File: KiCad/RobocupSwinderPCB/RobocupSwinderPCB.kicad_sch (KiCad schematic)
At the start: 29 parts, among them J1 Barrel_Jack, M1 Stepper_Motor_bipolar, M2 Stepper_Motor_bipolar, SW1 Limit_Switch, SW2 Limit_Switch, SW3 SW_SPST, U1 Teensy4.1, U3 LM7805_TO220

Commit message: Pcb cleanup
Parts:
- U1: footprint TeensyLibrary:Teensy41-Pins-Only_Silkscreen -> SwinderFootprintLibrary:Teensy41-Pins-Only_Silkscreen
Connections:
- net LCD_SCL_Pin_19: now also LCD1.3 (SDA); no longer LCD1.4 (SCL)
- net LCD_SDA_Pin_18: now also LCD1.4 (SCL); no longer LCD1.3 (SDA)
- net RE_CLK_Pin_23: now also RE1.3 (CLK); no longer RE1.5 (SW)
- net RE_SW_Pin_21: now also RE1.5 (SW); no longer RE1.3 (CLK)

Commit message: More pcb cleanup.
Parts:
- J1: footprint Library:CUI_PJ-037A -> SwinderFootprintLibrary:CUI_PJ-037A
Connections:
- net LCD_SCL_Pin_19: now also LCD1.4 (SCL); no longer LCD1.3 (SDA)
- net LCD_SDA_Pin_18: now also LCD1.3 (SDA); no longer LCD1.4 (SCL)
- net PWR_SW_OUT: now reaches F1.1, SW3.2 (B)
- net PWR_SW_IN: now reaches J1.1, SW3.1 (A)
- net RE_CLK_Pin_23 renamed RE_CLK_Pin_21
- net RE_CLK_Pin_21: now also U1.43 (21_A7_RX5_BCLK1); no longer U1.45 (23_A9_CRX1_MCLK1)
- net RE_SW_Pin_21 renamed RE_SW_Pin_23
- net RE_SW_Pin_23: now also U1.45 (23_A9_CRX1_MCLK1); no longer U1.43 (21_A7_RX5_BCLK1)
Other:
- note added: "Control"
- note added: "Front I/O"
- note added: "Internal Inputs"
- note added: "Motor Drivers"
- note removed: "Control and I/O"
- moved on the sheet: A1, A2, C1, C2, C3, C4, C5, D1, D2, F1, H1, H2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

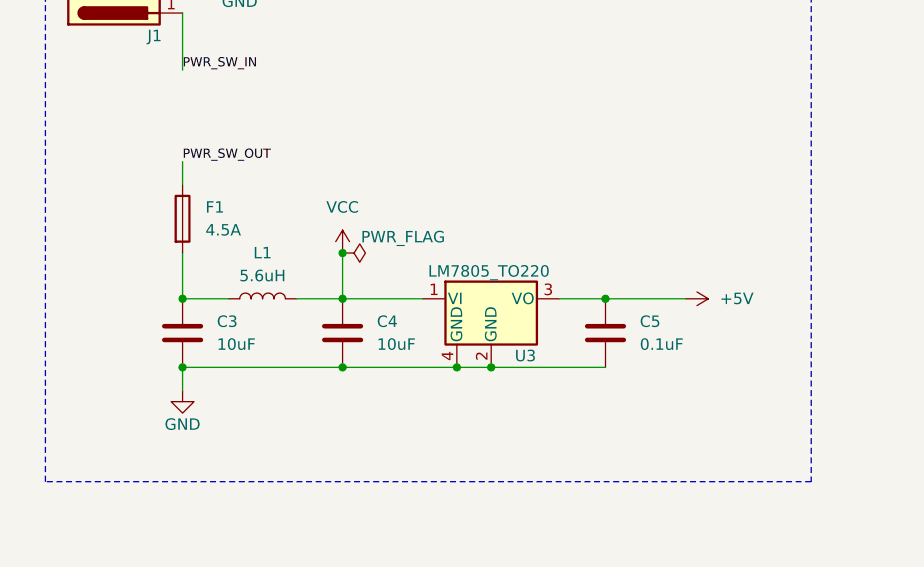
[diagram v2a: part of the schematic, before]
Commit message: Removed filter inductor and cap.
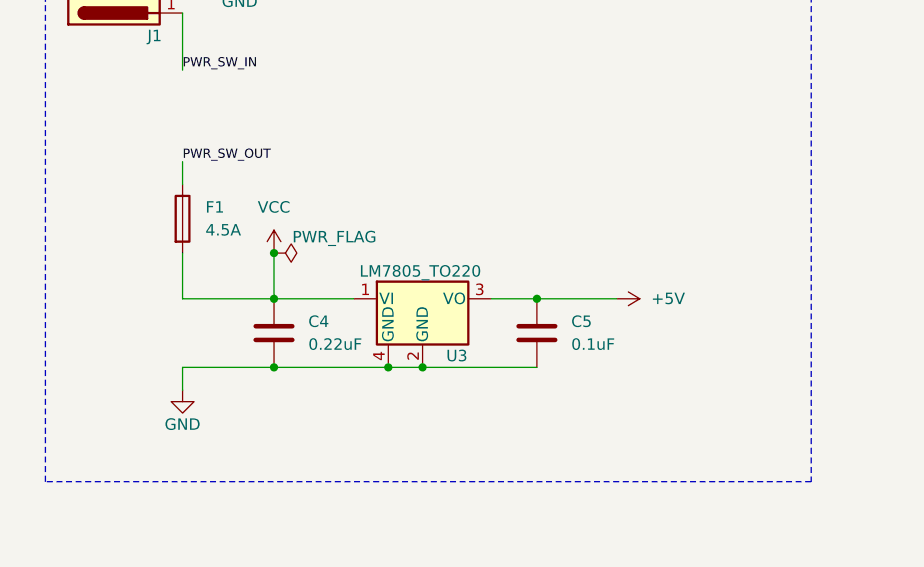
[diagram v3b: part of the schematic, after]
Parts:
- removed C3: 10uF, Capacitor_SMD:C_1206_3216Metric_Pad1.33x1.80mm_HandSolder, symbol Device:C
- removed L1: 5.6uH, Inductor_SMD:L_TracoPower_TCK-141, symbol Device:L
- C4: value 10uF -> 0.22uF
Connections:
- net VCC: now also F1.2
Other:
- moved on the sheet: C4, C5, U3

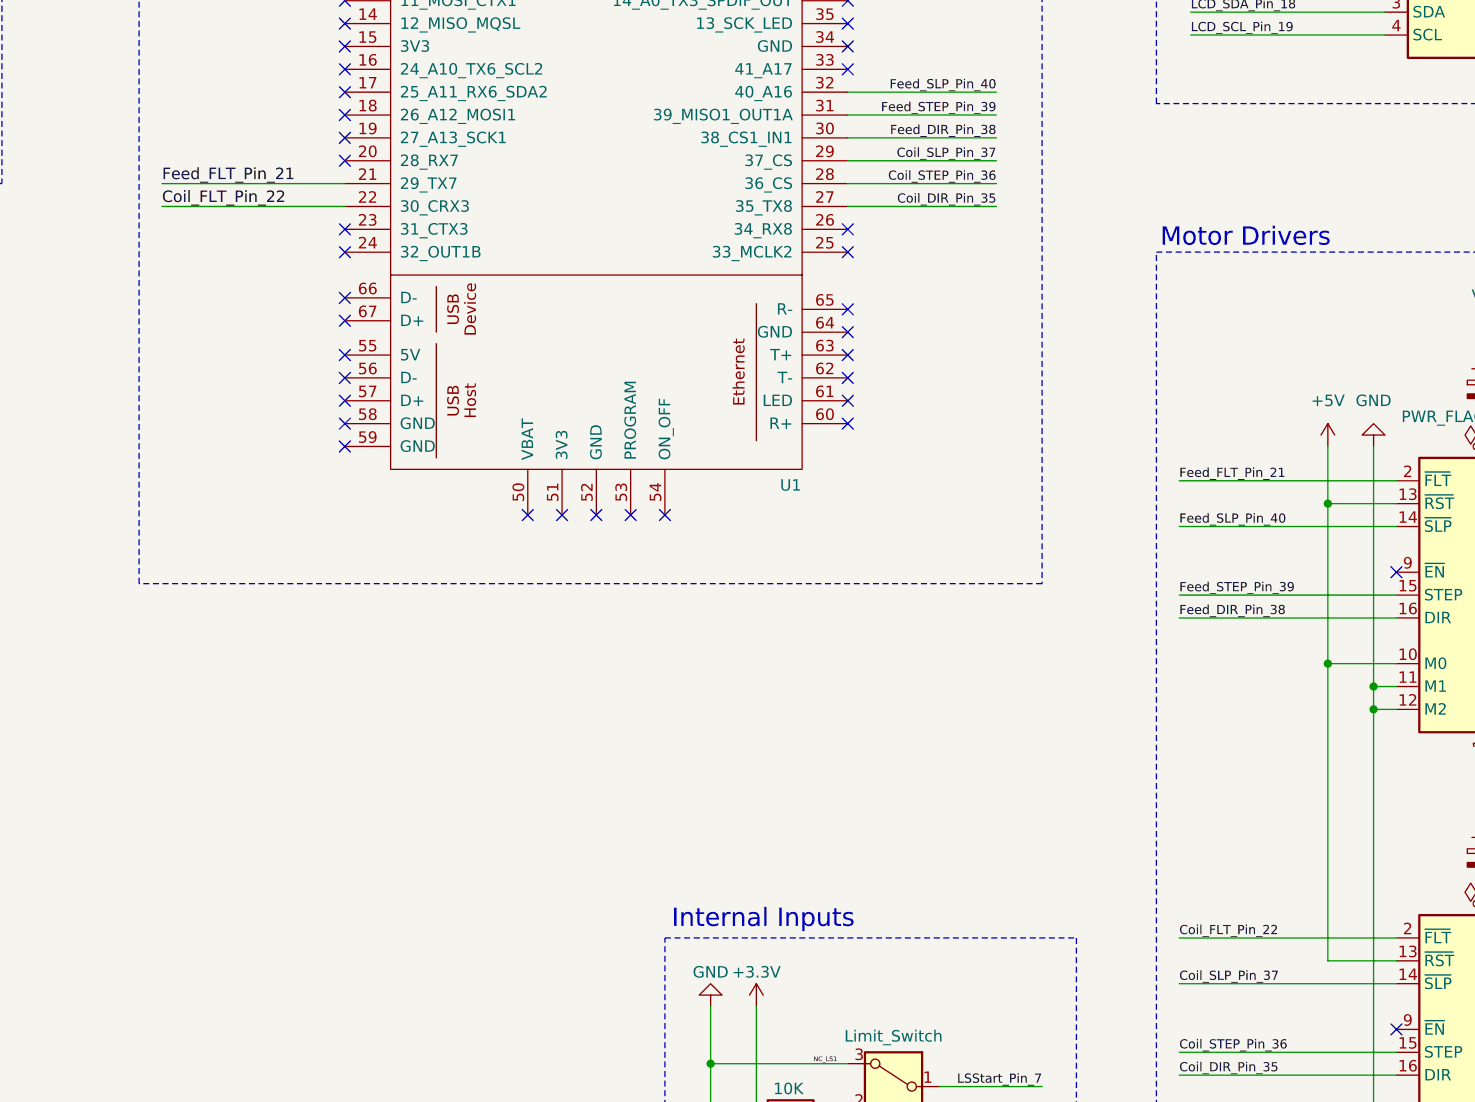
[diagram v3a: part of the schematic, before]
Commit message: fixed pin name.
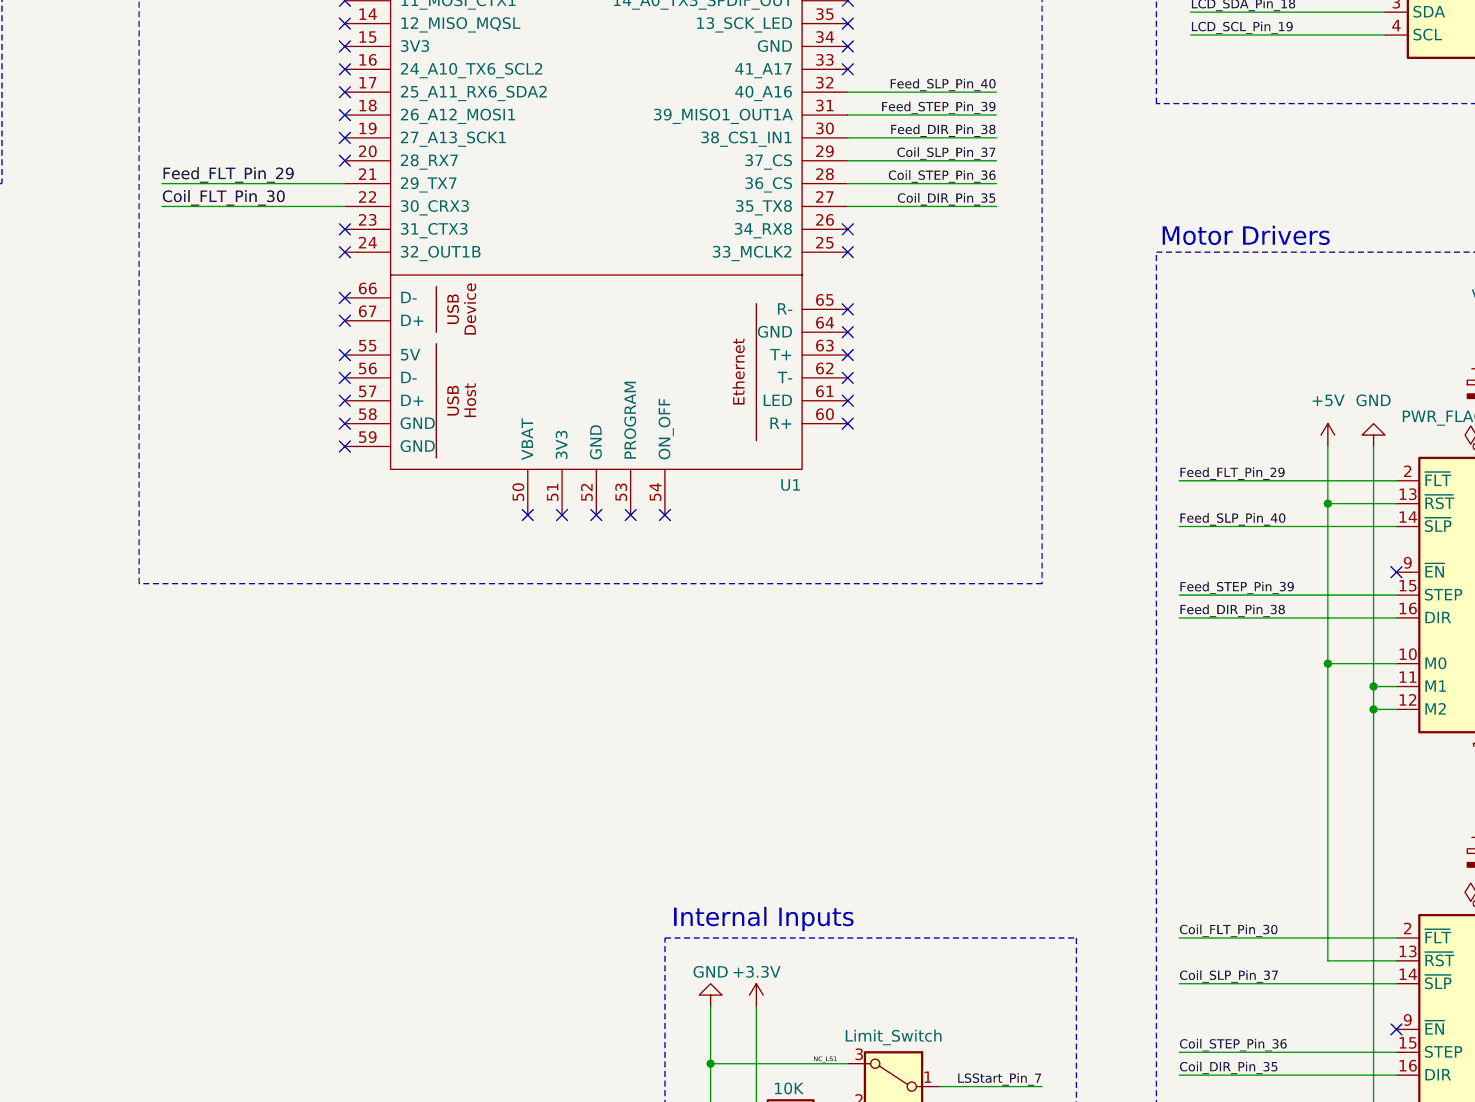
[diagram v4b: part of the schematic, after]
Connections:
- net Coil_FLT_Pin_22 renamed Coil_FLT_Pin_30
- net Feed_FLT_Pin_21 renamed Feed_FLT_Pin_29
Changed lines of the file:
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@@
 		)
 	)
-	(label "Feed_FLT_Pin_21"
+	(label "Feed_FLT_Pin_29"
 		(at 276.86 132.08 0)
 		(effects
@@
 		)
 	)
-	(label "Coil_FLT_Pin_22"
+	(label "Coil_FLT_Pin_30"
 		(at 276.86 182.88 0)
 		(effects
@@
 		)
 	)
-	(label "Feed_FLT_Pin_21"
+	(label "Feed_FLT_Pin_29"
 		(at 163.83 99.06 0)
 		(effects
@@
 		)
 	)
-	(label "Coil_FLT_Pin_22"
+	(label "Coil_FLT_Pin_30"
 		(at 163.83 101.6 0)
 		(effects

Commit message: Final commit till v1.0
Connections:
- net GND: now also C1.2, C2.2
- net VCC: now also A1.8 (VMOT), A2.8 (VMOT)
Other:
- moved on the sheet: C1, C2
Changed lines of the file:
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@@
 	)
 	(junction
-		(at 311.15 177.8)
+		(at 66.04 184.15)
 		(diameter 0)
 		(color 0 0 0 0)
 	)
 	(junction
-		(at 66.04 184.15)
+		(at 298.45 154.94)
 		(diameter 0)
 		(color 0 0 0 0)
 	)
 	(junction
-		(at 298.45 154.94)
+		(at 298.45 128.27)
 		(diameter 0)
 		(color 0 0 0 0)
 	)
 	(junction
-		(at 311.15 127)
+		(at 311.15 172.72)
 		(diameter 0)
 		(color 0 0 0 0)
@@
 	)
 	(junction
-		(at 311.15 118.11)
+		(at 313.69 165.1)
 		(diameter 0)
 		(color 0 0 0 0)
 	)
 	(junction
-		(at 313.69 165.1)
+		(at 311.15 120.65)
 		(diameter 0)
 		(color 0 0 0 0)
@@
 	)
 	(junction
+		(at 298.45 172.72)
+		(diameter 0)
+		(color 0 0 0 0)
+	)
+	(junction
 		(at 313.69 215.9)
 		(diameter 0)
@@
 	)
 	(junction
+		(at 311.15 177.8)
+		(diameter 0)
+		(color 0 0 0 0)
+	)
+	(junction
 		(at 115.57 78.74)
 		(diameter 0)
@@
 	)
 	(junction
+		(at 311.15 127)
+		(diameter 0)
+		(color 0 0 0 0)
+	)
+	(junction
+		(at 311.15 118.11)
+		(diameter 0)
+		(color 0 0 0 0)
+	)
+	(junction
 		(at 298.45 203.2)
 		(diameter 0)
@@
 	(wire
 		(pts
-			(xy 298.45 203.2) (xy 298.45 157.48)
+			(xy 298.45 203.2) (xy 298.45 172.72)
+		)
+		(stroke
+			(width 0)
+			(type default)
+		)
+	)
+	(wire
+		(pts
+			(xy 298.45 172.72) (xy 298.45 157.48)
 		)
 		(stroke
@@
 	(wire
 		(pts
+			(xy 298.45 172.72) (xy 303.53 172.72)
+		)
+		(stroke
+			(width 0)
+			(type default)
+		)
+	)
+	(wire
+		(pts
 			(xy 76.2 86.36) (xy 86.36 86.36)
 		)
@@
 	(wire
 		(pts
+			(xy 311.15 172.72) (xy 311.15 177.8)
+		)
+		(stroke
+			(width 0)
+			(type default)
+		)
+	)
+	(wire
+		(pts
 			(xy 240.03 48.26) (xy 243.84 48.26)
 		)
@@
 	(wire
 		(pts
-			(xy 311.15 167.64) (xy 311.15 170.18)
+			(xy 311.15 167.64) (xy 311.15 172.72)
 		)
 		(stroke
@@
 	(wire
 		(pts
+			(xy 311.15 118.11) (xy 311.15 120.65)
+		)
+		(stroke
+			(width 0)
+			(type default)
+		)
+	)
+	(wire
+		(pts
 			(xy 76.2 46.99) (xy 76.2 53.34)
 		)
@@
 	(wire
 		(pts
-			(xy 311.15 125.73) (xy 311.15 127)
-		)
-		(stroke
-			(width 0)
-			(type default)
-		)
-	)
-	(wire
-		(pts
 			(xy 96.52 134.62) (xy 99.06 134.62)
 		)
@@
 	(wire
 		(pts
+			(xy 303.53 120.65) (xy 303.53 128.27)
+		)
+		(stroke
+			(width 0)
+			(type default)
+		)
+	)
+	(wire
+		(pts
 			(xy 311.15 165.1) (xy 311.15 162.56)
 		)
@@
 	(wire
 		(pts
+			(xy 303.53 128.27) (xy 298.45 128.27)
+		)
+		(stroke
+			(width 0)
+			(type default)
+		)
+	)
+	(wire
+		(pts
 			(xy 240.03 88.9) (xy 256.54 88.9)
 		)
@@
 	(wire
 		(pts
+			(xy 311.15 120.65) (xy 311.15 127)
+		)
+		(stroke
+			(width 0)
+			(type default)
+		)
+	)
+	(wire
+		(pts
 			(xy 163.83 63.5) (xy 184.15 63.5)
 		)
@@
 	(symbol
 		(lib_id "Device:C_Polarized")
-		(at 311.15 173.99 0)
+		(at 307.34 172.72 270)
 		(unit 1)
 		(exclude_from_sim no)
@@
 		(fields_autoplaced yes)
 		(property "Reference" "C2"
-			(at 314.96 171.8309 0)
+			(at 308.229 165.1 90)
 			(effects
 				(font
 					(size 1.27 1.27)
 				)
-				(justify left)
 			)
 		)
 		(property "Value" "100uF"
-			(at 314.96 174.3709 0)
+			(at 308.229 167.64 90)
 			(effects
 				(font
 					(size 1.27 1.27)
 				)
-				(justify left)
 			)
 		)
 		(property "Footprint" "Capacitor_THT:CP_Radial_D8.0mm_P3.50mm"
-			(at 312.1152 177.8 0)
+			(at 303.53 173.6852 0)
 			(effects
 				(font
@@
 		)
 		(property "Datasheet" "~"
-			(at 311.15 173.99 0)
+			(at 307.34 172.72 0)
 			(effects
 				(font
@@
 		)
 		(property "Description" "Polarized capacitor"
-			(at 311.15 173.99 0)
+			(at 307.34 172.72 0)
 			(effects
 				(font
@@
 	(symbol
 		(lib_id "Device:C_Polarized")
-		(at 311.15 121.92 0)
+		(at 307.34 120.65 270)
 		(unit 1)
 		(exclude_from_sim no)
@@
 		(fields_autoplaced yes)
 		(property "Reference" "C1"
-			(at 314.96 119.7609 0)
+			(at 308.229 113.03 90)
 			(effects
 				(font
 					(size 1.27 1.27)
 				)
-				(justify left)
 			)
 		)
 		(property "Value" "100uF"
-			(at 314.96 122.3009 0)
+			(at 308.229 115.57 90)
 			(effects
 				(font
 					(size 1.27 1.27)
 				)
-				(justify left)
 			)
 		)
 		(property "Footprint" "Capacitor_THT:CP_Radial_D8.0mm_P3.50mm"
-			(at 312.1152 125.73 0)
+			(at 303.53 121.6152 0)
 			(effects
 				(font
@@
 		)
 		(property "Datasheet" "~"
-			(at 311.15 121.92 0)
+			(at 307.34 120.65 0)
 			(effects
 				(font
@@
 		)
 		(property "Description" "Polarized capacitor"
-			(at 311.15 121.92 0)
+			(at 307.34 120.65 0)
 			(effects
 				(font
